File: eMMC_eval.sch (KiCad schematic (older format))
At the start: 10 parts, among them J1 Conn_01x03_Male, J2 Conn_01x04_Male, J3 Conn_01x10_Male, J4 eMMC Module, J5 Conn_01x03_Male, J6 Conn_01x03_Male, J7 Conn_01x10_Male, J8 Conn_01x05_Male, J9 Conn_01x05_Male

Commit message: WIP before back-annotation test
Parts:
- removed J4: eMMC Module, Connector_PinHeader_1.27mm:PinHeader_2x10_P1.27mm_Vertical, symbol Connector_Generic:Conn_02x10_Odd_Even
- removed J5: Conn_01x03_Male, Connector_PinHeader_2.54mm:PinHeader_1x03_P2.54mm_Vertical, symbol Connector:Conn_01x03_Male
- removed J8, J9: Conn_01x05_Male, Connector_PinHeader_2.54mm:PinHeader_1x05_P2.54mm_Vertical, symbol Connector:Conn_01x05_Male
- removed JP1: SolderJumper_2_Bridged, Jumper:SolderJumper-2_P1.3mm_Bridged_RoundedPad1.0x1.5mm, symbol Jumper:SolderJumper_2_Bridged
- added C1: 2.2uF 6.3V, Capacitor_SMD:C_0603_1608Metric, symbol Device:CP1_Small
- added J6: Conn_01x04_Male, Connector_PinSocket_2.54mm:PinSocket_1x04_P2.54mm_Vertical, symbol Connector:Conn_01x04_Female
- added U1: THGBMNG5D1LBAIT, BGA153N50P14X14_1000X1100X80, symbol eMMC_eval-rescue:THGBMNG5D1LBAIT-THGBMNG5D1LBAIT
- renumbered J6 to J4, J7 to J5
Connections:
- net labels added: SPI1-CLK, SPI1-MISO, SPI1-MOSI, ~SDMMC1_RST, ~SPI1-NSS
- net labels removed: RESET, RESET_x, STRB, STRB_x, VCC_IO
- wire segments 82 -> 48
- no-connect marks 8 -> 4
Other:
- note added: "(15)"
- note added: "(6)"
- note added: "Remove Nucleo SB21 to free up\nSPI1-CLK on PA5"
- note added: "SPI port to Apollo"
- note removed: "The signal VCC_IO is an unknown, if it should\nNOT be connected the 3V3, open this bridge."
- note removed: "These signals are not used by\nstm32f452 SDMMC module. These\nlinks allow them to be driven by the\nMCU, or jumpered to VCc or GND."
- moved on the sheet: J1, J2, J3, J4, J5

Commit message: eMMC chip symbol updated and pushed to PCB
Has all NC pins remapped to the signals the PCB needs to use to escape the BGA
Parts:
- U1: symbol eMMC_eval-rescue:THGBMNG5D1LBAIT-THGBMNG5D1LBAIT -> eMMC_eval:THGBMNG5D1LBAIT-THGBMNG5D1LBAIT
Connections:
- net +3V3: now also U1.A9 (VCCQ), U1.B8 (VCCQ), U1.C7 (VCCQ)
- net GND: now also U1.D3 (VSSQ), U1.E2 (VSSQ), U1.F1 (VSSQ), U1.P1 (VSSQ)
- net SDMMC1_CK: now also U1.N7 (CLK), U1.P8 (CLK)
- net SDMMC1_CMD: now also U1.L1 (CMD), U1.L2 (CMD), U1.L3 (CMD)
- net SDMMC1_D3: now also U1.A1 (DAT3)
- net SDMMC1_D4: now also U1.A2 (DAT4)
- net SDMMC1_D5: now also U1.C3 (DAT5), U1.D2 (DAT5), U1.E1 (DAT5)
- net SDMMC1_D6: now also U1.C5 (DAT6), U1.D4 (DAT6), U1.E3 (DAT6), U1.F2 (DAT6), U1.G1 (DAT6)
- net SDMMC1_D7: now also U1.A8 (DAT7), U1.B7 (DAT7)
- net ~SDMMC1_RST: now also U1.L12 (~RST), U1.L13 (~RST), U1.L14 (~RST)
- net at U1.C1 (VDDI): now also C1.1, U1.C2 (VDDI)
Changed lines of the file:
@@
 $EndComp
 $Comp
-L eMMC_eval-rescue:THGBMNG5D1LBAIT-THGBMNG5D1LBAIT U1
+L eMMC_eval:THGBMNG5D1LBAIT-THGBMNG5D1LBAIT U1
 U 1 1 5F7D2D84
 P 6250 3150

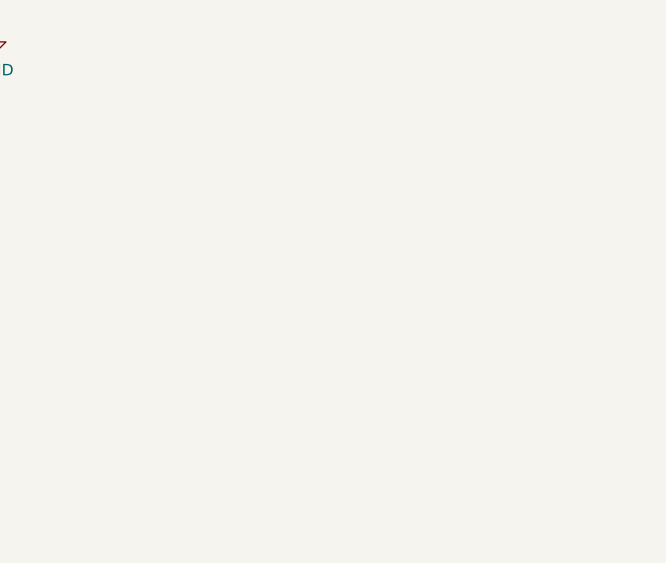
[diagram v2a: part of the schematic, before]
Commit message: Fixed SPI header to be pins, added 3D model for eMMC
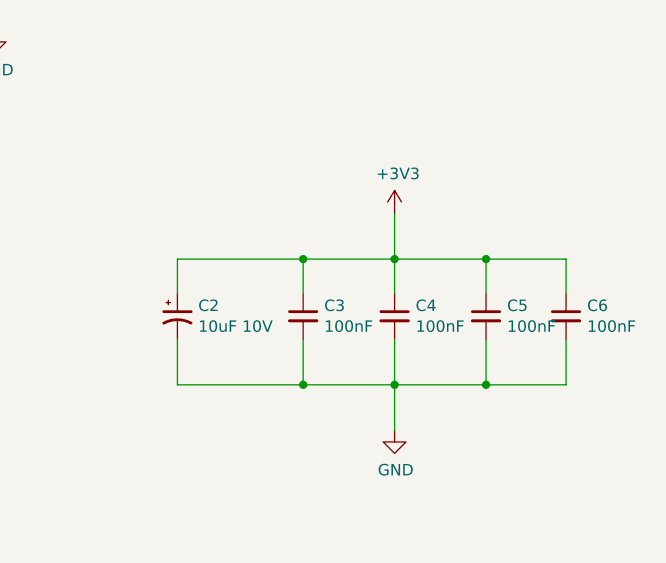
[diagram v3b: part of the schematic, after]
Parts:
- added C2: 10uF 10V, Capacitor_SMD:C_0603_1608Metric, symbol Device:CP1_Small
- added C3, C4, C5, C6: 100nF, Capacitor_SMD:C_0603_1608Metric, symbol Device:C_Small
- J6: footprint Connector_PinSocket_2.54mm:PinSocket_1x04_P2.54mm_Vertical -> Connector_PinHeader_2.54mm:PinHeader_1x04_P2.54mm_Vertical
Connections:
- net +3V3: now also C2.1, C3.1, C4.1, C5.1, C6.1
- net GND: now also C2.2, C3.2, C4.2, C5.2, C6.2
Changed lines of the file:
@@
 F 0 "J6" H 2600 6050 50  0000 C CNN
 F 1 "Conn_01x04_Male" H 2708 5990 50  0001 C CNN
-F 2 "Connector_PinSocket_2.54mm:PinSocket_1x04_P2.54mm_Vertical" H 2600 5800 50  0001 C CNN
+F 2 "Connector_PinHeader_2.54mm:PinHeader_1x04_P2.54mm_Vertical" H 2600 5800 50  0001 C CNN
 F 3 "~" H 2600 5800 50  0001 C CNN
 	1    2600 5800
@@
 $EndComp
 NoConn ~ 6950 2650
+$Comp
+L Device:CP1_Small C2
+U 1 1 5F80189F
+P 7950 5250
+F 0 "C2" H 8041 5296 50  0000 L CNN
+F 1 "10uF 10V" H 8041 5205 50  0000 L CNN
+F 2 "Capacitor_SMD:C_0603_1608Metric" H 7950 5250 50  0001 C CNN
+F 3 "~" H 7950 5250 50  0001 C CNN
+	1    7950 5250
+	1    0    0    -1
+$EndComp
+$Comp
+L Device:C_Small C3
+U 1 1 5F8025BD
+P 8500 5250
+F 0 "C3" H 8592 5296 50  0000 L CNN
+F 1 "100nF" H 8592 5205 50  0000 L CNN
+F 2 "Capacitor_SMD:C_0603_1608Metric" H 8500 5250 50  0001 C CNN
+F 3 "~" H 8500 5250 50  0001 C CNN
+	1    8500 5250
+	1    0    0    -1
+$EndComp
+$Comp
+L Device:C_Small C4
+U 1 1 5F802FDF
+P 8900 5250
+F 0 "C4" H 8992 5296 50  0000 L CNN
+F 1 "100nF" H 8992 5205 50  0000 L CNN
+F 2 "Capacitor_SMD:C_0603_1608Metric" H 8900 5250 50  0001 C CNN
+F 3 "~" H 8900 5250 50  0001 C CNN
+	1    8900 5250
+	1    0    0    -1
+$EndComp
+$Comp
+L Device:C_Small C5
+U 1 1 5F80310F
+P 9300 5250
+F 0 "C5" H 9392 5296 50  0000 L CNN
+F 1 "100nF" H 9392 5205 50  0000 L CNN
+F 2 "Capacitor_SMD:C_0603_1608Metric" H 9300 5250 50  0001 C CNN
+F 3 "~" H 9300 5250 50  0001 C CNN
+	1    9300 5250
+	1    0    0    -1
+$EndComp
+$Comp
+L Device:C_Small C6
+U 1 1 5F80323A
+P 9650 5250
+F 0 "C6" H 9742 5296 50  0000 L CNN
+F 1 "100nF" H 9742 5205 50  0000 L CNN
+F 2 "Capacitor_SMD:C_0603_1608Metric" H 9650 5250 50  0001 C CNN
+F 3 "~" H 9650 5250 50  0001 C CNN
+	1    9650 5250
+	1    0    0    -1
+$EndComp
+Wire Wire Line
+	7950 5150 7950 5000
+Wire Wire Line
+	7950 5000 8500 5000
+Wire Wire Line
+	9650 5000 9650 5150
+Wire Wire Line
+	9300 5150 9300 5000
+Connection ~ 9300 5000
+Wire Wire Line
+	9300 5000 9650 5000
+Wire Wire Line
+	8900 5000 8900 5150
+Connection ~ 8900 5000
+Wire Wire Line
+	8900 5000 9300 5000
+Wire Wire Line
+	8500 5150 8500 5000
+Connection ~ 8500 5000
+Wire Wire Line
+	8500 5000 8900 5000
+Wire Wire Line
+	7950 5350 7950 5550
+Wire Wire Line
+	7950 5550 8500 5550
+Wire Wire Line
+	9650 5550 9650 5350
+Wire Wire Line
+	9300 5350 9300 5550
+Connection ~ 9300 5550
+Wire Wire Line
+	9300 5550 9650 5550
+Wire Wire Line
+	8900 5550 8900 5350
+Connection ~ 8900 5550
+Wire Wire Line
+	8900 5550 9300 5550
+Wire Wire Line
+	8500 5350 8500 5550
+Connection ~ 8500 5550
+Wire Wire Line
+	8500 5550 8900 5550
+Wire Wire Line
+	8900 5550 8900 5750
+Wire Wire Line
+	8900 5000 8900 4800
+$Comp
+L power:GND #PWR06
+U 1 1 5F810754
+P 8900 5750
+F 0 "#PWR06" H 8900 5500 50  0001 C CNN
+F 1 "GND" H 8905 5577 50  0000 C CNN
+F 2 "" H 8900 5750 50  0001 C CNN
+F 3 "" H 8900 5750 50  0001 C CNN
+	1    8900 5750
+	1    0    0    -1
+$EndComp
+$Comp
+L power:+3V3 #PWR05
+U 1 1 5F810E20
+P 8900 4800
+F 0 "#PWR05" H 8900 4650 50  0001 C CNN
+F 1 "+3V3" H 8915 4973 50  0000 C CNN
+F 2 "" H 8900 4800 50  0001 C CNN
+F 3 "" H 8900 4800 50  0001 C CNN
+	1    8900 4800
+	1    0    0    -1
+$EndComp
 $EndSCHEMATC

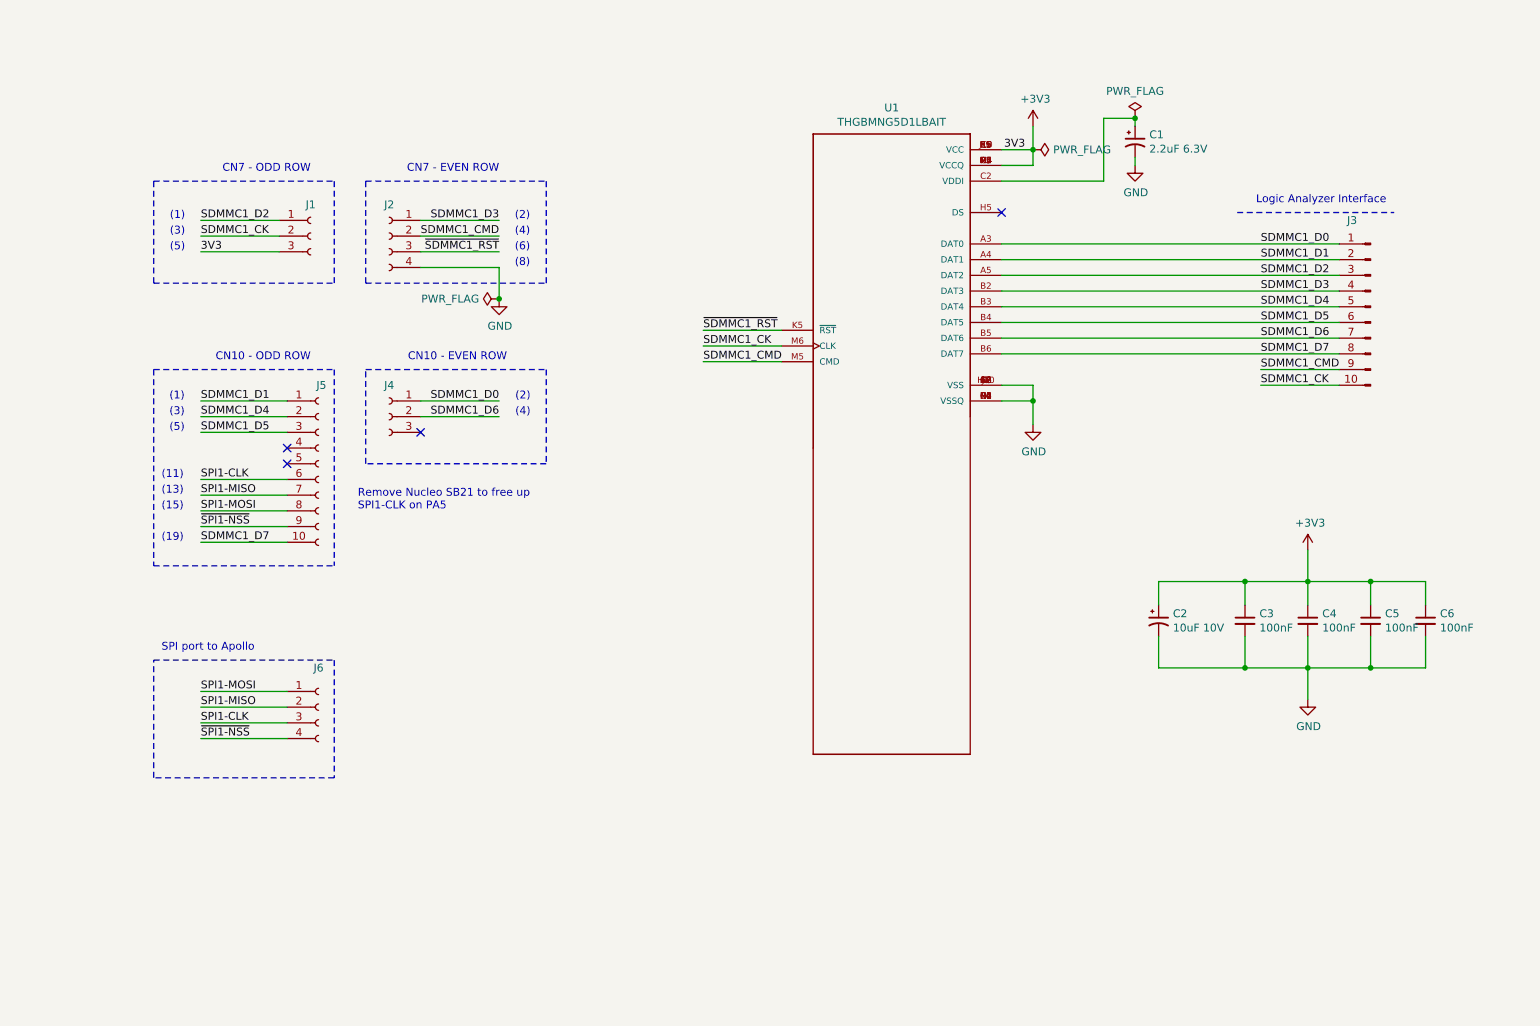
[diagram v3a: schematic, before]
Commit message: Added pullup resistors and fixed issue with reset input
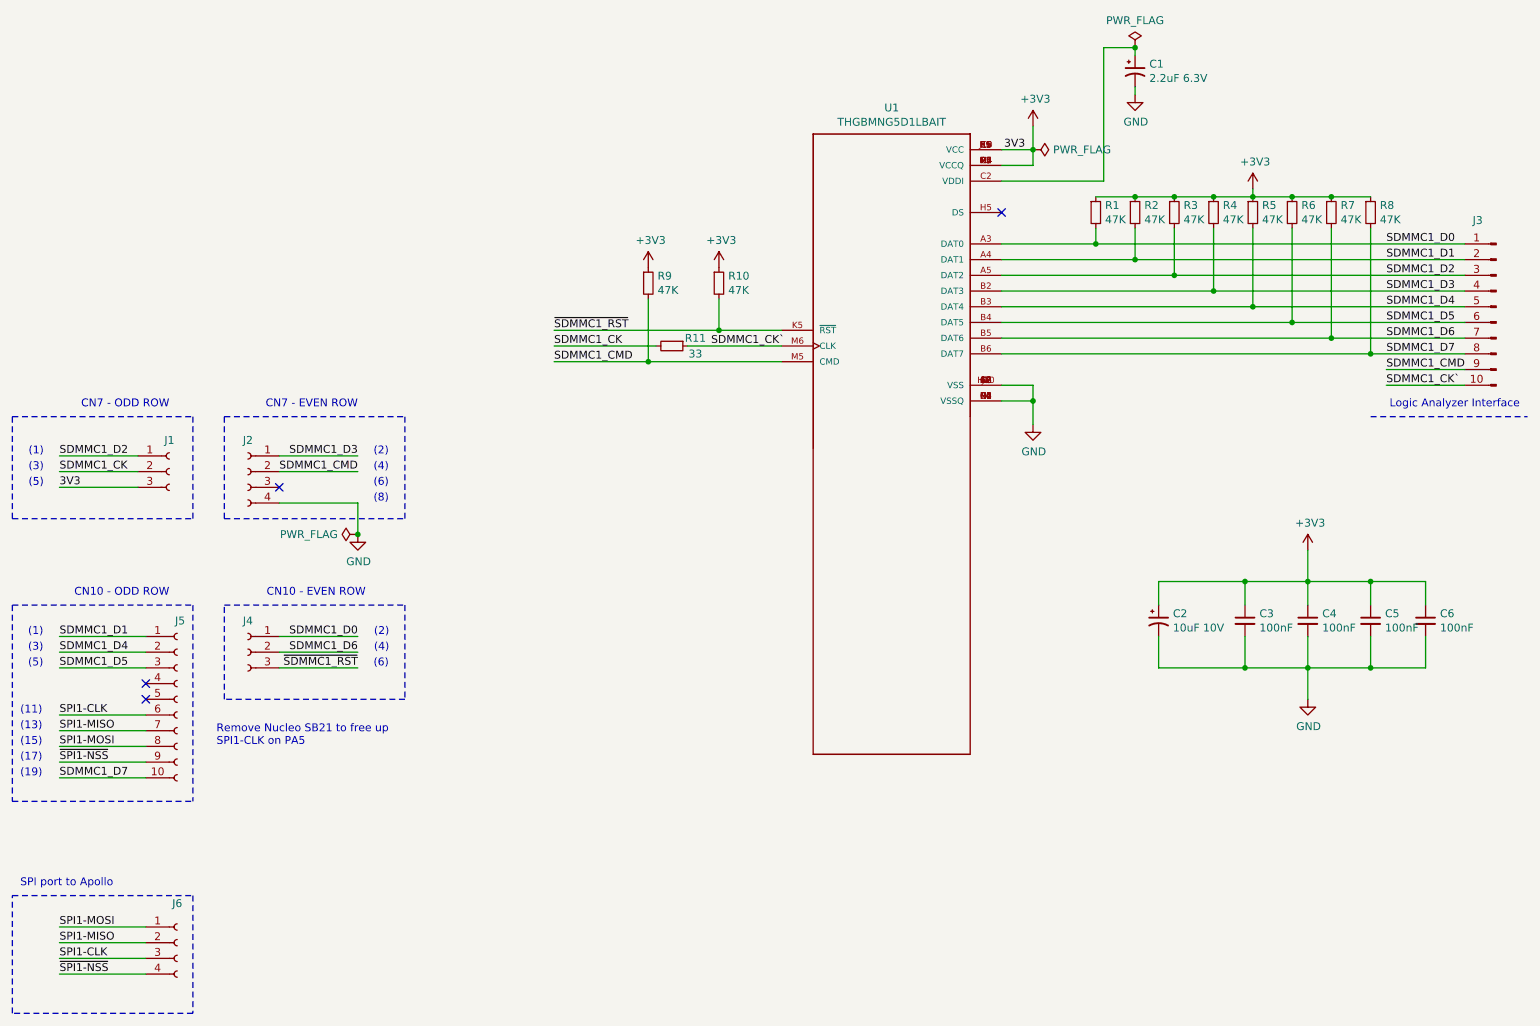
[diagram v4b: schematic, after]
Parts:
- added R1, R10, R2, R3, R4, R5, R6, R7, R8, R9: 47K, Resistor_SMD:R_0805_2012Metric, symbol Device:R_Small
- added R11: 33, Resistor_SMD:R_0805_2012Metric, symbol Device:R_Small
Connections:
- net +3V3: now also R1.1, R10.1, R2.1, R3.1, R4.1, R5.1, R6.1, R7.1, R8.1, R9.1
- net SDMMC1_CK: now also R11.2; no longer J3.10 (Pin_10), U1.M6 (CLK), U1.N7 (CLK), U1.P8 (CLK)
- net SDMMC1_CMD: now also R9.2
- net SDMMC1_D0: now also R1.2
- net SDMMC1_D1: now also R2.2
- net SDMMC1_D2: now also R3.2
- net SDMMC1_D3: now also R4.2
- net SDMMC1_D4: now also R5.2
- net SDMMC1_D5: now also R6.2
- net SDMMC1_D6: now also R7.2
- net SDMMC1_D7: now also R8.2
- net ~SDMMC1_RST: now also J4.3 (Pin_3), R10.2; no longer J2.3 (Pin_3)
- new net SDMMC1_CK`: J3.10 (Pin_10), R11.1, U1.M6 (CLK), U1.N7 (CLK), U1.P8 (CLK)
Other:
- note added: "(17)"
- moved on the sheet: C1, J1, J2, J3, J4, J5, J6

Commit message: Value change on CMD pullup
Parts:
- R9: value 47K -> 10K
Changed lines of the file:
@@
 Title "eMMC chip Evaluation Board"
 Date "2020-10-05"
-Rev "1.0"
+Rev "1.0a"
 Comp "Sid Price Design"
-Comment1 ""
+Comment1 "1.0a, changed CMD pullup to 10K"
 Comment2 ""
 Comment3 ""
@@
 P 4700 3100
 F 0 "R9" H 4759 3146 50  0000 L CNN
-F 1 "47K" H 4759 3055 50  0000 L CNN
+F 1 "10K" H 4759 3055 50  0000 L CNN
 F 2 "Resistor_SMD:R_0805_2012Metric" H 4700 3100 50  0001 C CNN
 F 3 "~" H 4700 3100 50  0001 C CNN
